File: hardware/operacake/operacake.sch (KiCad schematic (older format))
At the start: 129 parts, among them J1 CONN_02X20, J2 CONN_02X20, P1 ADDRESS, P20 GPIO, P22 I2S, P28 SD, P9 BASEBAND, U1 MASWSS0129, U10 74LVC1G58, U11 74LVC1G58, U12 74LVC1G58, U13 74LVC1G58, U14 74AHC1G02, U15 74AHC1G02, U16 74LVC1G19, U2 SKY13322, U3 SKY13322, U4 PCA9557, U5 TC7MBL3245CFT, U6 74LVC1G58, U7 74LVC1G58, U8 74AHC1G08, U9 74AHC1G08

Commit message: Added decoupling capacitors.
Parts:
- added C13, C14, C15, C16, C17, C18, C19, C20, C21, C22: 33pF, gsg-modules:0402, symbol C
- added C23, C24, C25, C26, C27, C28, C29, C30, C31, C32, C33: 100nF, gsg-modules:0402, symbol C
- C1, C10, C11, C12, C2, C3, C4, C5, C6, C7, C8, C9: value C -> 100nF
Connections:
- net GND: now also C13.2, C14.2, C15.1, C16.1, C17.1, C18.1, C19.2, C20.2, C21.1, C22.1, C23.1, C24.1, C25.1, C26.1, C27.1, C28.1, C29.1, C30.1, C31.1, C32.1, C33.1
- net U1VC1: now also C18.2
- net U1VC2: now also C17.2
- net U2V1: now also C14.1
- net U2V2: now also C15.2
- net U2V3: now also C13.1
- net U2V4: now also C16.2
- net U3V1: now also C20.1
- net U3V2: now also C21.2
- net U3V3: now also C19.1
- net U3V4: now also C22.2
- net VCC: now also C23.2, C24.2, C25.2, C26.2, C27.2, C28.2, C29.2, C30.2, C31.2, C32.2, C33.2
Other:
- moved on the sheet: C10, C9, U14, U15, U6, U7

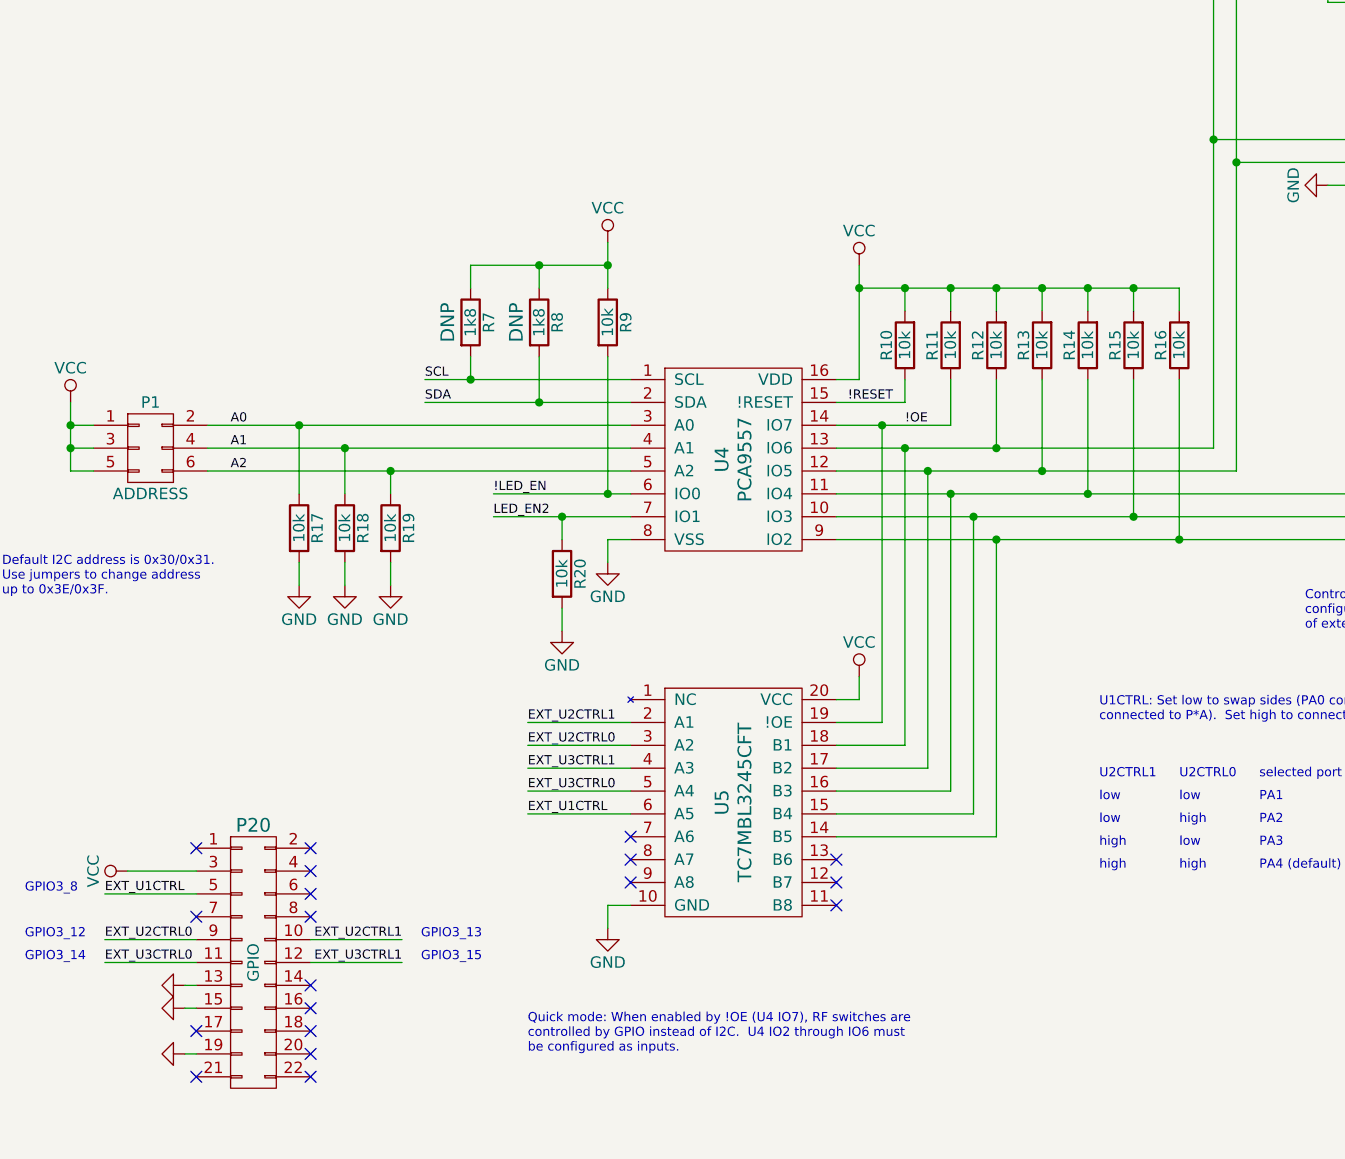
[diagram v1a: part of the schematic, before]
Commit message: more decoupling caps and remove one GND from P22
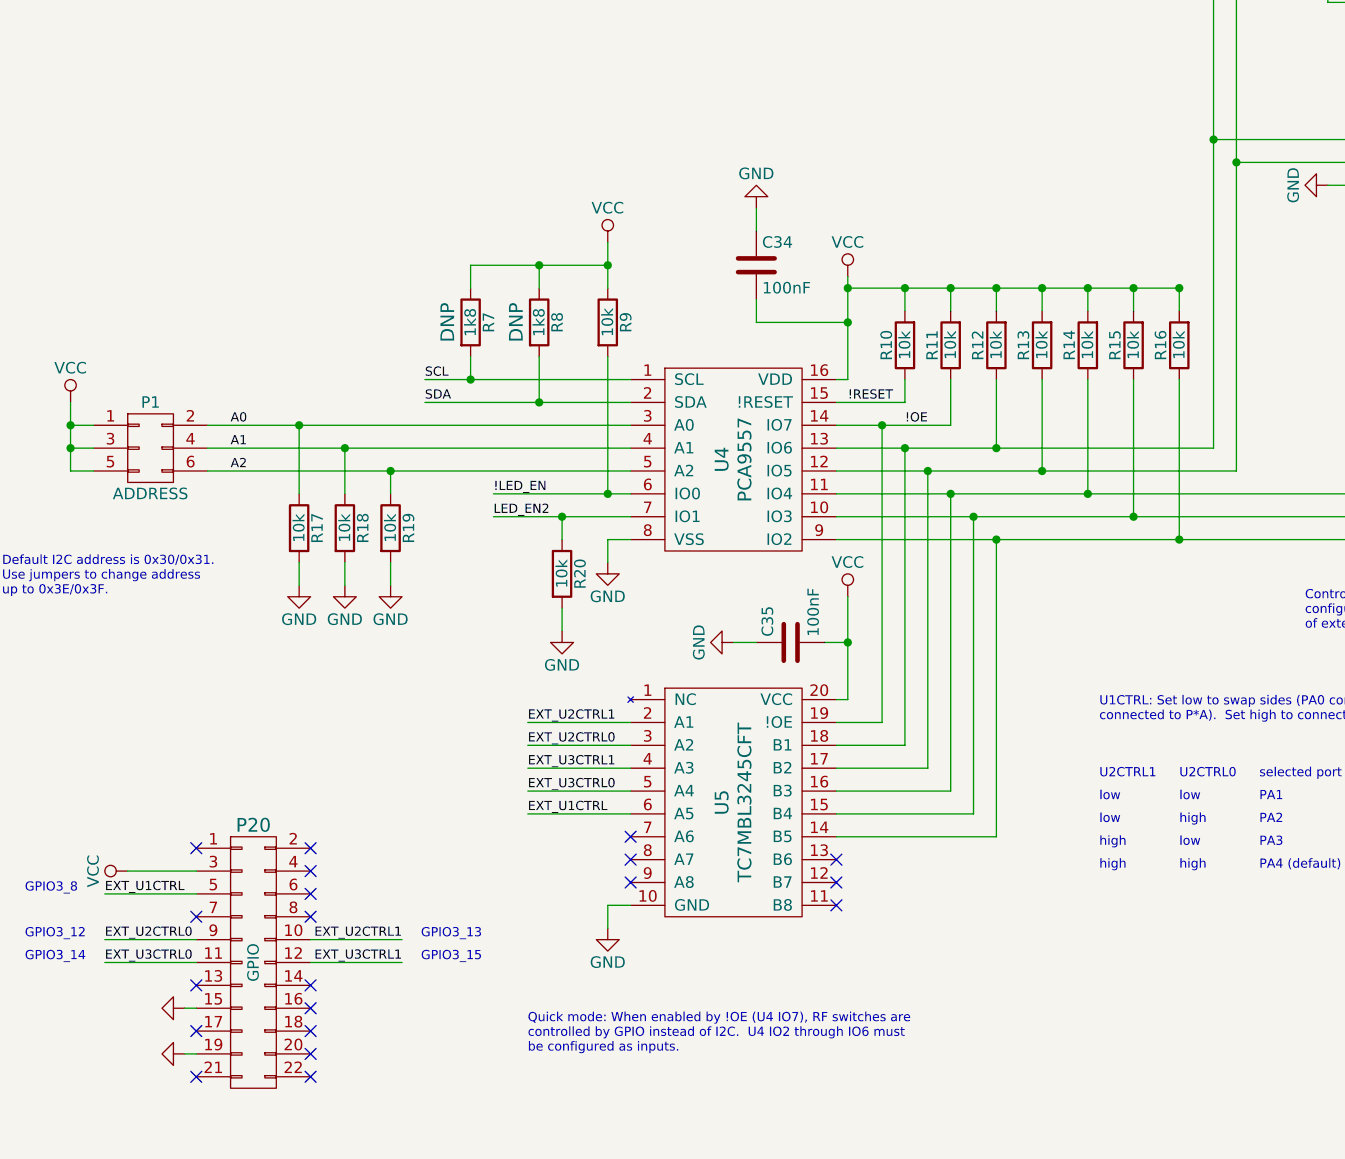
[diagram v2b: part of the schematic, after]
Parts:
- added C34, C35: 100nF, gsg-modules:0402, symbol C
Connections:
- net GND: now also C34.1, C35.1; no longer P20.13 (P13)
- net VCC: now also C34.2, C35.2
- no-connect marks 136 -> 137

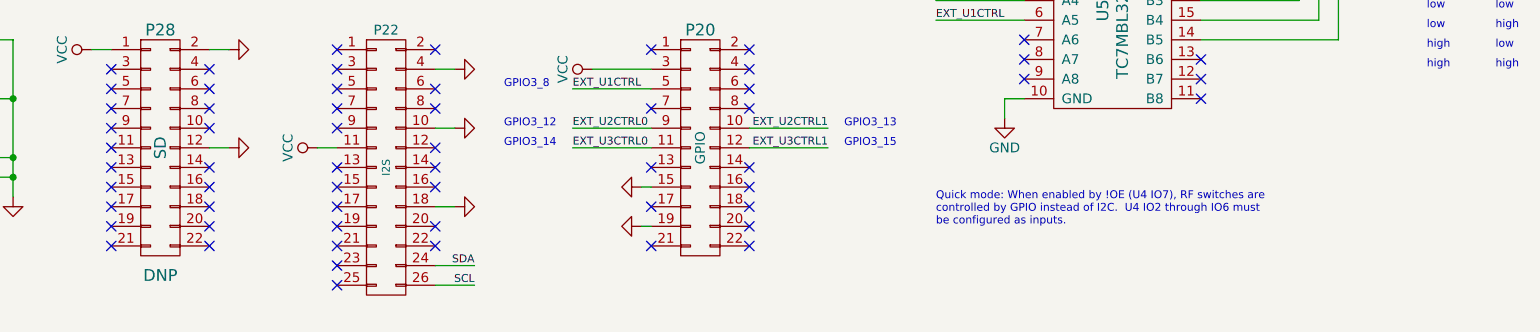
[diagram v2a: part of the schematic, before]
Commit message: Opera Cake: pin header part selection
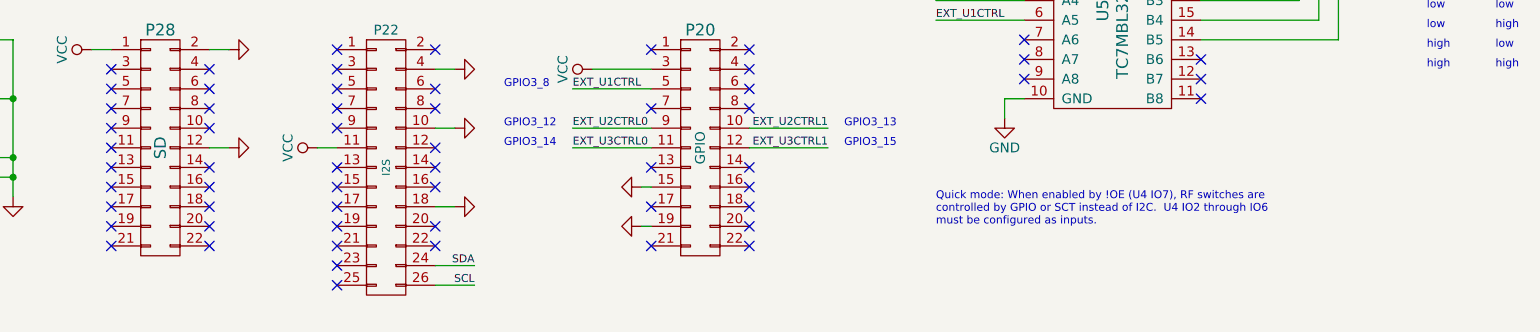
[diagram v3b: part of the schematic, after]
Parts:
- P1: Description (none) -> JUMPER PLUG 6POS DOUBLE ROW; Manufacturer (none) -> Omron; Part Number (none) -> XG8T-0631
- P20: Desciption (none) -> CONN RCPT .100\" 22POS DUAL GOLD; Manufacturer (none) -> Samtec; Part Number (none) -> SSQ-111-03-G-D
- P22: Description (none) -> CONN RCPT .100\" 26POS DUAL GOLD; Manufacturer (none) -> Samtec; Part Number (none) -> SSQ-113-03-G-D
- P28: Description (none) -> CONN RCPT .100\" 22POS DUAL GOLD; Manufacturer (none) -> Samtec; Note DNP -> (none); Part Number (none) -> SSQ-111-03-G-D
- P9: Description (none) -> CONN RCPT .100\" 16POS DUAL GOLD; Manufacturer (none) -> Samtec; Part Number (none) -> SSQ-108-03-G-D
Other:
- note added: "Quick mode: When enabled by !OE (U4 IO7), RF switches are\ncontrolled by GPIO or SCT instead of I2C. U4 IO2 through IO6\nmust be configured as inputs."
- note removed: "Quick mode: When enabled by !OE (U4 IO7), RF switches are\ncontrolled by GPIO instead of I2C. U4 IO2 through IO6 must\nbe configured as inputs."
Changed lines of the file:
@@
 F 2 "gsg-modules:HEADER-2x11" H 5550 9500 60  0001 C CNN
 F 3 "" H 5550 9500 60  0001 C CNN
-F 4 "DNP" H 5550 8850 60  0000 C CNN "Note"
+F 4 "Samtec" H 5550 9500 60  0001 C CNN "Manufacturer"
+F 5 "SSQ-111-03-G-D" H 5550 9500 60  0001 C CNN "Part Number"
+F 6 "CONN RCPT .100\" 22POS DUAL GOLD" H 5550 9500 60  0001 C CNN "Description"
 	1    5550 9500
 	1    0    0    -1
@@
 F 2 "gsg-modules:HEADER-2x13" H 6700 9600 60  0001 C CNN
 F 3 "" H 6700 9600 60  0001 C CNN
+F 4 "Samtec" H 6700 9600 60  0001 C CNN "Manufacturer"
+F 5 "SSQ-113-03-G-D" H 6700 9600 60  0001 C CNN "Part Number"
+F 6 "CONN RCPT .100\" 26POS DUAL GOLD" H 6700 9600 60  0001 C CNN "Description"
 	1    6700 9600
 	1    0    0    -1
@@
 F 2 "gsg-modules:HEADER-2x11" H 8300 9500 60  0001 C CNN
 F 3 "" H 8300 9500 60  0001 C CNN
+F 4 "Samtec" H 8300 9500 60  0001 C CNN "Manufacturer"
+F 5 "SSQ-111-03-G-D" H 8300 9500 60  0001 C CNN "Part Number"
+F 6 "CONN RCPT .100\" 22POS DUAL GOLD" H 8300 9500 60  0001 C CNN "Desciption"
 	1    8300 9500
 	1    0    0    -1
@@
 F 2 "gsg-modules:HEADER-2x3" H 7850 6050 60  0001 C CNN
 F 3 "" H 7850 6050 60  0000 C CNN
+F 4 "Omron" H 7850 7250 60  0001 C CNN "Manufacturer"
+F 5 "XG8T-0631" H 7850 7250 60  0001 C CNN "Part Number"
+F 6 "JUMPER PLUG 6POS DOUBLE ROW" H 7850 7250 60  0001 C CNN "Description"
 	1    7850 7250
 	1    0    0    -1
@@
 F 2 "gsg-modules:HEADER-2x8" H 4450 8100 60  0001 C CNN
 F 3 "" H 4450 8100 60  0000 C CNN
-F 4 "DNP" H 4450 8800 60  0000 C CNN "Note"
+F 4 "Samtec" H 4450 9300 60  0001 C CNN "Manufacturer"
+F 5 "SSQ-108-03-G-D" H 4450 9300 60  0001 C CNN "Part Number"
+F 6 "CONN RCPT .100\" 16POS DUAL GOLD" H 4450 9300 60  0001 C CNN "Description"
+F 7 "DNP" H 4450 8800 60  0000 C CNN "Note"
 	1    4450 9300
 	1    0    0    -1
@@
 test points
 Text Notes 9500 9900 0    40   ~ 0
-Quick mode: When enabled by !OE (U4 IO7), RF switches are\ncontrolled by GPIO instead of I2C.  U4 IO2 through IO6 must\nbe configured as inputs.
+Quick mode: When enabled by !OE (U4 IO7), RF switches are\ncontrolled by GPIO or SCT instead of I2C.  U4 IO2 through IO6\nmust be configured as inputs.
 Text Notes 12900 8050 0    40   ~ 0
 Control logic guarantees valid RF switch\nconfiguration and reduces the number\nof external control signals required.
